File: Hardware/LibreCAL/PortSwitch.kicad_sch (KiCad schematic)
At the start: 20 parts, among them J1 901-10510-2, J2 901-10510-2, J3 901-10510-2, J4 901-10510-2, U1 PE426462, U2 PE426462, U3 PE426462, U4 PE426462

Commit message: Partial routing
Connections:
- net GND: now also U1.20 (NC), U2.20 (NC), U3.20 (NC), U4.20 (NC)
- net at U2.2 (RF2): now also U3.2 (RF2); no longer U4.15 (RF4)
- net at U2.4 (RF3): now also U4.15 (RF4); no longer U3.4 (RF3)
- net at U1.15 (RF4): now also U3.4 (RF3); no longer U3.2 (RF2)
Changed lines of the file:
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@@
   (junction (at 207.01 142.24) (diameter 0) (color 0 0 0 0)
   )
+  (junction (at 72.39 66.04) (diameter 0) (color 0 0 0 0)
+  )
   (junction (at 212.09 142.24) (diameter 0) (color 0 0 0 0)
   )
@@
   (junction (at 100.33 76.2) (diameter 0) (color 0 0 0 0)
   )
+  (junction (at 219.71 66.04) (diameter 0) (color 0 0 0 0)
+  )
   (junction (at 207.01 76.2) (diameter 0) (color 0 0 0 0)
   )
@@
   (junction (at 196.85 76.2) (diameter 0) (color 0 0 0 0)
   )
+  (junction (at 72.39 132.08) (diameter 0) (color 0 0 0 0)
+  )
   (junction (at 92.71 100.33) (diameter 0) (color 0 0 0 0)
   )
@@
   )
   (junction (at 191.77 142.24) (diameter 0) (color 0 0 0 0)
+  )
+  (junction (at 219.71 132.08) (diameter 0) (color 0 0 0 0)
   )
   (junction (at 186.69 142.24) (diameter 0) (color 0 0 0 0)
@@
     (stroke (width 0) (type default) (color 0 0 0 0))
   )
+  (wire (pts (xy 113.03 124.46) (xy 138.43 124.46))
+    (stroke (width 0) (type default) (color 0 0 0 0))
+  )
   (wire (pts (xy 97.79 142.24) (xy 95.25 142.24))
     (stroke (width 0) (type default) (color 0 0 0 0))
@@
     (stroke (width 0) (type default) (color 0 0 0 0))
   )
+  (wire (pts (xy 156.21 58.42) (xy 179.07 58.42))
+    (stroke (width 0) (type default) (color 0 0 0 0))
+  )
   (wire (pts (xy 97.79 140.97) (xy 97.79 142.24))
     (stroke (width 0) (type default) (color 0 0 0 0))
@@
     (stroke (width 0) (type default) (color 0 0 0 0))
   )
-  (wire (pts (xy 156.21 60.96) (xy 156.21 55.88))
-    (stroke (width 0) (type default) (color 0 0 0 0))
-  )
   (wire (pts (xy 179.07 60.96) (xy 161.29 60.96))
     (stroke (width 0) (type default) (color 0 0 0 0))
   )
+  (wire (pts (xy 179.07 55.88) (xy 151.13 55.88))
+    (stroke (width 0) (type default) (color 0 0 0 0))
+  )
+  (wire (pts (xy 72.39 132.08) (xy 74.93 132.08))
+    (stroke (width 0) (type default) (color 0 0 0 0))
+  )
   (wire (pts (xy 102.87 76.2) (xy 100.33 76.2))
     (stroke (width 0) (type default) (color 0 0 0 0))
   )
-  (wire (pts (xy 156.21 55.88) (xy 179.07 55.88))
-    (stroke (width 0) (type default) (color 0 0 0 0))
-  )
   (wire (pts (xy 222.25 63.5) (xy 217.17 63.5))
     (stroke (width 0) (type default) (color 0 0 0 0))
@@
     (stroke (width 0) (type default) (color 0 0 0 0))
   )
+  (wire (pts (xy 72.39 66.04) (xy 74.93 66.04))
+    (stroke (width 0) (type default) (color 0 0 0 0))
+  )
   (wire (pts (xy 199.39 34.29) (xy 199.39 46.99))
     (stroke (width 0) (type default) (color 0 0 0 0))
@@
     (stroke (width 0) (type default) (color 0 0 0 0))
   )
-  (wire (pts (xy 72.39 55.88) (xy 72.39 76.2))
+  (wire (pts (xy 72.39 55.88) (xy 72.39 66.04))
     (stroke (width 0) (type default) (color 0 0 0 0))
   )
@@
     (stroke (width 0) (type default) (color 0 0 0 0))
   )
-  (wire (pts (xy 151.13 58.42) (xy 179.07 58.42))
-    (stroke (width 0) (type default) (color 0 0 0 0))
-  )
-  (wire (pts (xy 219.71 55.88) (xy 219.71 76.2))
+  (wire (pts (xy 113.03 121.92) (xy 138.43 121.92))
+    (stroke (width 0) (type default) (color 0 0 0 0))
+  )
+  (wire (pts (xy 219.71 66.04) (xy 219.71 76.2))
+    (stroke (width 0) (type default) (color 0 0 0 0))
+  )
+  (wire (pts (xy 219.71 55.88) (xy 219.71 66.04))
     (stroke (width 0) (type default) (color 0 0 0 0))
   )
@@
     (stroke (width 0) (type default) (color 0 0 0 0))
   )
+  (wire (pts (xy 72.39 66.04) (xy 72.39 76.2))
+    (stroke (width 0) (type default) (color 0 0 0 0))
+  )
+  (wire (pts (xy 138.43 121.92) (xy 138.43 63.5))
+    (stroke (width 0) (type default) (color 0 0 0 0))
+  )
   (wire (pts (xy 92.71 74.93) (xy 92.71 76.2))
     (stroke (width 0) (type default) (color 0 0 0 0))
@@
     (stroke (width 0) (type default) (color 0 0 0 0))
   )
+  (wire (pts (xy 138.43 124.46) (xy 138.43 127))
+    (stroke (width 0) (type default) (color 0 0 0 0))
+  )
   (wire (pts (xy 90.17 76.2) (xy 87.63 76.2))
     (stroke (width 0) (type default) (color 0 0 0 0))
@@
     (stroke (width 0) (type default) (color 0 0 0 0))
   )
-  (wire (pts (xy 113.03 124.46) (xy 138.43 124.46))
-    (stroke (width 0) (type default) (color 0 0 0 0))
-  )
   (wire (pts (xy 130.81 127) (xy 113.03 127))
     (stroke (width 0) (type default) (color 0 0 0 0))
@@
     (stroke (width 0) (type default) (color 0 0 0 0))
   )
-  (wire (pts (xy 179.07 127) (xy 148.59 127))
+  (wire (pts (xy 138.43 127) (xy 179.07 127))
     (stroke (width 0) (type default) (color 0 0 0 0))
   )
@@
     (stroke (width 0) (type default) (color 0 0 0 0))
   )
+  (wire (pts (xy 217.17 66.04) (xy 219.71 66.04))
+    (stroke (width 0) (type default) (color 0 0 0 0))
+  )
   (wire (pts (xy 199.39 100.33) (xy 199.39 113.03))
     (stroke (width 0) (type default) (color 0 0 0 0))
@@
     (stroke (width 0) (type default) (color 0 0 0 0))
   )
+  (wire (pts (xy 72.39 132.08) (xy 72.39 142.24))
+    (stroke (width 0) (type default) (color 0 0 0 0))
+  )
   (wire (pts (xy 74.93 119.38) (xy 48.26 119.38))
     (stroke (width 0) (type default) (color 0 0 0 0))
@@
     (stroke (width 0) (type default) (color 0 0 0 0))
   )
-  (wire (pts (xy 138.43 124.46) (xy 138.43 63.5))
-    (stroke (width 0) (type default) (color 0 0 0 0))
-  )
   (wire (pts (xy 90.17 140.97) (xy 90.17 142.24))
     (stroke (width 0) (type default) (color 0 0 0 0))
@@
     (stroke (width 0) (type default) (color 0 0 0 0))
   )
-  (wire (pts (xy 151.13 63.5) (xy 151.13 58.42))
+  (wire (pts (xy 151.13 55.88) (xy 151.13 63.5))
     (stroke (width 0) (type default) (color 0 0 0 0))
   )
@@
     (stroke (width 0) (type default) (color 0 0 0 0))
   )
+  (wire (pts (xy 219.71 132.08) (xy 219.71 142.24))
+    (stroke (width 0) (type default) (color 0 0 0 0))
+  )
   (wire (pts (xy 199.39 140.97) (xy 199.39 142.24))
     (stroke (width 0) (type default) (color 0 0 0 0))
@@
     (stroke (width 0) (type default) (color 0 0 0 0))
   )
-  (wire (pts (xy 148.59 127) (xy 148.59 121.92))
+  (wire (pts (xy 217.17 132.08) (xy 219.71 132.08))
     (stroke (width 0) (type default) (color 0 0 0 0))
   )
@@
     (stroke (width 0) (type default) (color 0 0 0 0))
   )
-  (wire (pts (xy 219.71 121.92) (xy 219.71 142.24))
+  (wire (pts (xy 219.71 121.92) (xy 219.71 132.08))
     (stroke (width 0) (type default) (color 0 0 0 0))
   )
@@
     (stroke (width 0) (type default) (color 0 0 0 0))
   )
+  (wire (pts (xy 156.21 58.42) (xy 156.21 60.96))
+    (stroke (width 0) (type default) (color 0 0 0 0))
+  )
   (wire (pts (xy 113.03 53.34) (xy 115.57 53.34))
     (stroke (width 0) (type default) (color 0 0 0 0))
@@
     (stroke (width 0) (type default) (color 0 0 0 0))
   )
-  (wire (pts (xy 148.59 121.92) (xy 113.03 121.92))
-    (stroke (width 0) (type default) (color 0 0 0 0))
-  )
   (wire (pts (xy 102.87 142.24) (xy 100.33 142.24))
     (stroke (width 0) (type default) (color 0 0 0 0))
@@
     (stroke (width 0) (type default) (color 0 0 0 0))
   )
-  (wire (pts (xy 72.39 121.92) (xy 72.39 142.24))
+  (wire (pts (xy 72.39 121.92) (xy 72.39 132.08))
     (stroke (width 0) (type default) (color 0 0 0 0))
   )
@@
     (pin "1")
   )
-  (symbol (lib_id "LibreCAL:PE426462") (at 92.71 124.46 0) (unit 1)
+  (symbol (lib_name "PE426462_2") (lib_id "LibreCAL:PE426462") (at 92.71 124.46 0) (unit 1)
     (in_bom yes) (on_board yes) (fields_autoplaced)
     (property "Reference" "U2" (id 0) (at 94.7294 110.49 0)
@@
     (pin "1")
   )
-  (symbol (lib_id "LibreCAL:PE426462") (at 92.71 58.42 0) (unit 1)
+  (symbol (lib_name "PE426462_1") (lib_id "LibreCAL:PE426462") (at 92.71 58.42 0) (unit 1)
     (in_bom yes) (on_board yes) (fields_autoplaced)
     (property "Reference" "U1" (id 0) (at 94.7294 44.45 0)
@@
     (pin "1")
   )
-  (symbol (lib_id "LibreCAL:PE426462") (at 199.39 58.42 0) (mirror y) (unit 1)
+  (symbol (lib_name "PE426462_3") (lib_id "LibreCAL:PE426462") (at 199.39 58.42 0) (mirror y) (unit 1)
     (in_bom yes) (on_board yes) (fields_autoplaced)
     (property "Reference" "U3" (id 0) (at 197.3706 44.45 0)

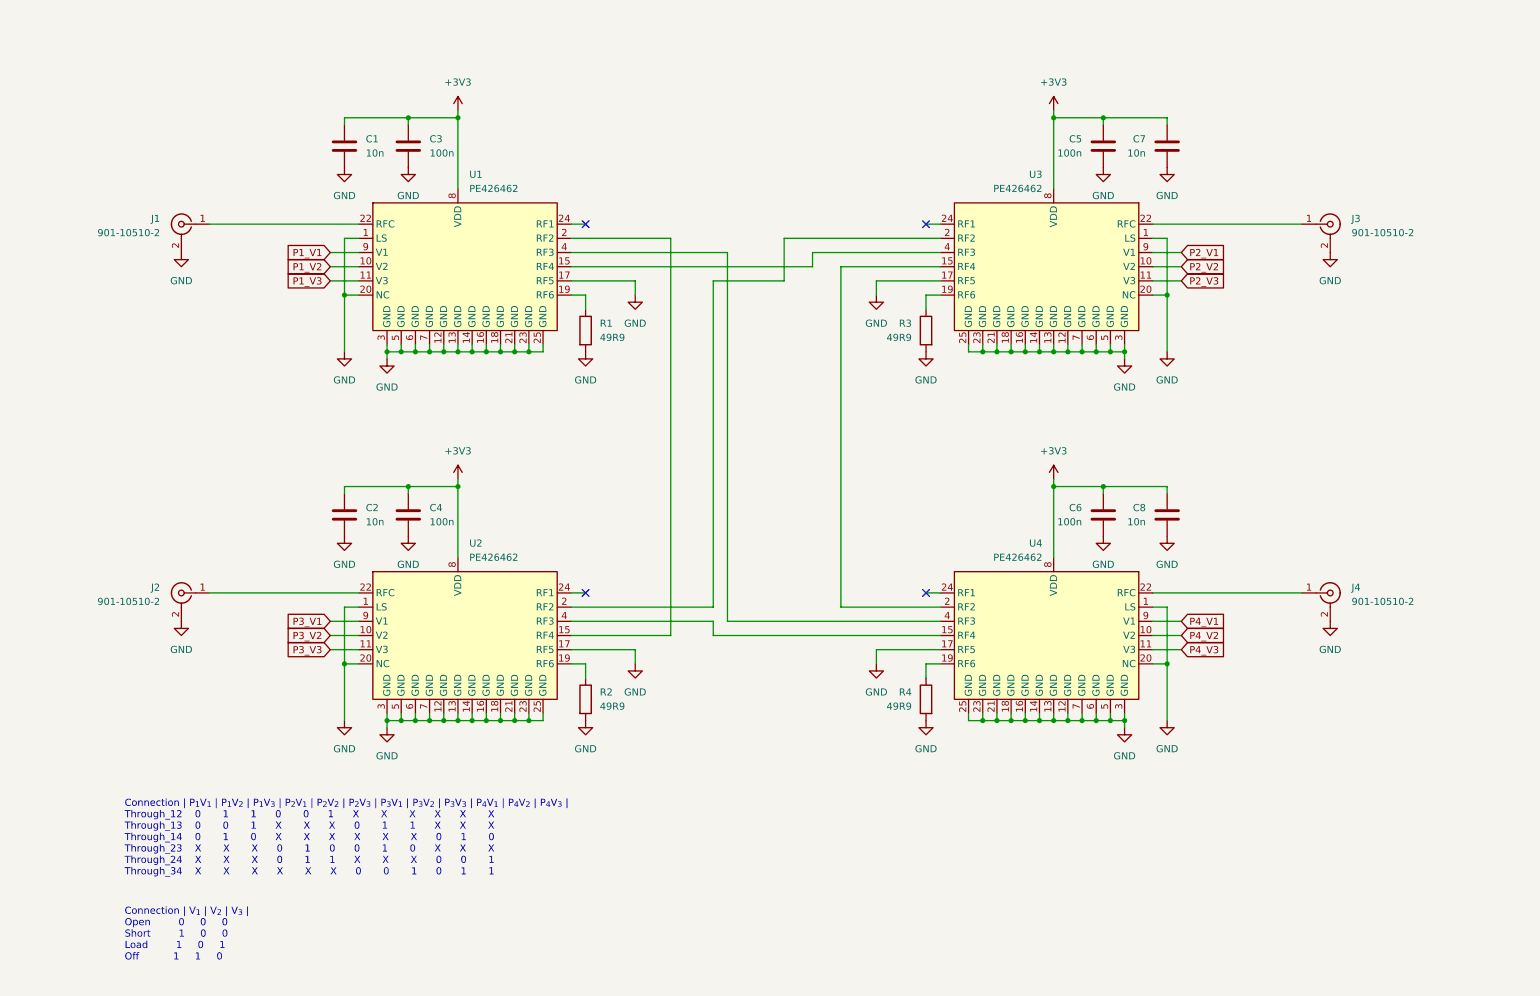
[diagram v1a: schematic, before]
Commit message: Filters added, housing updated
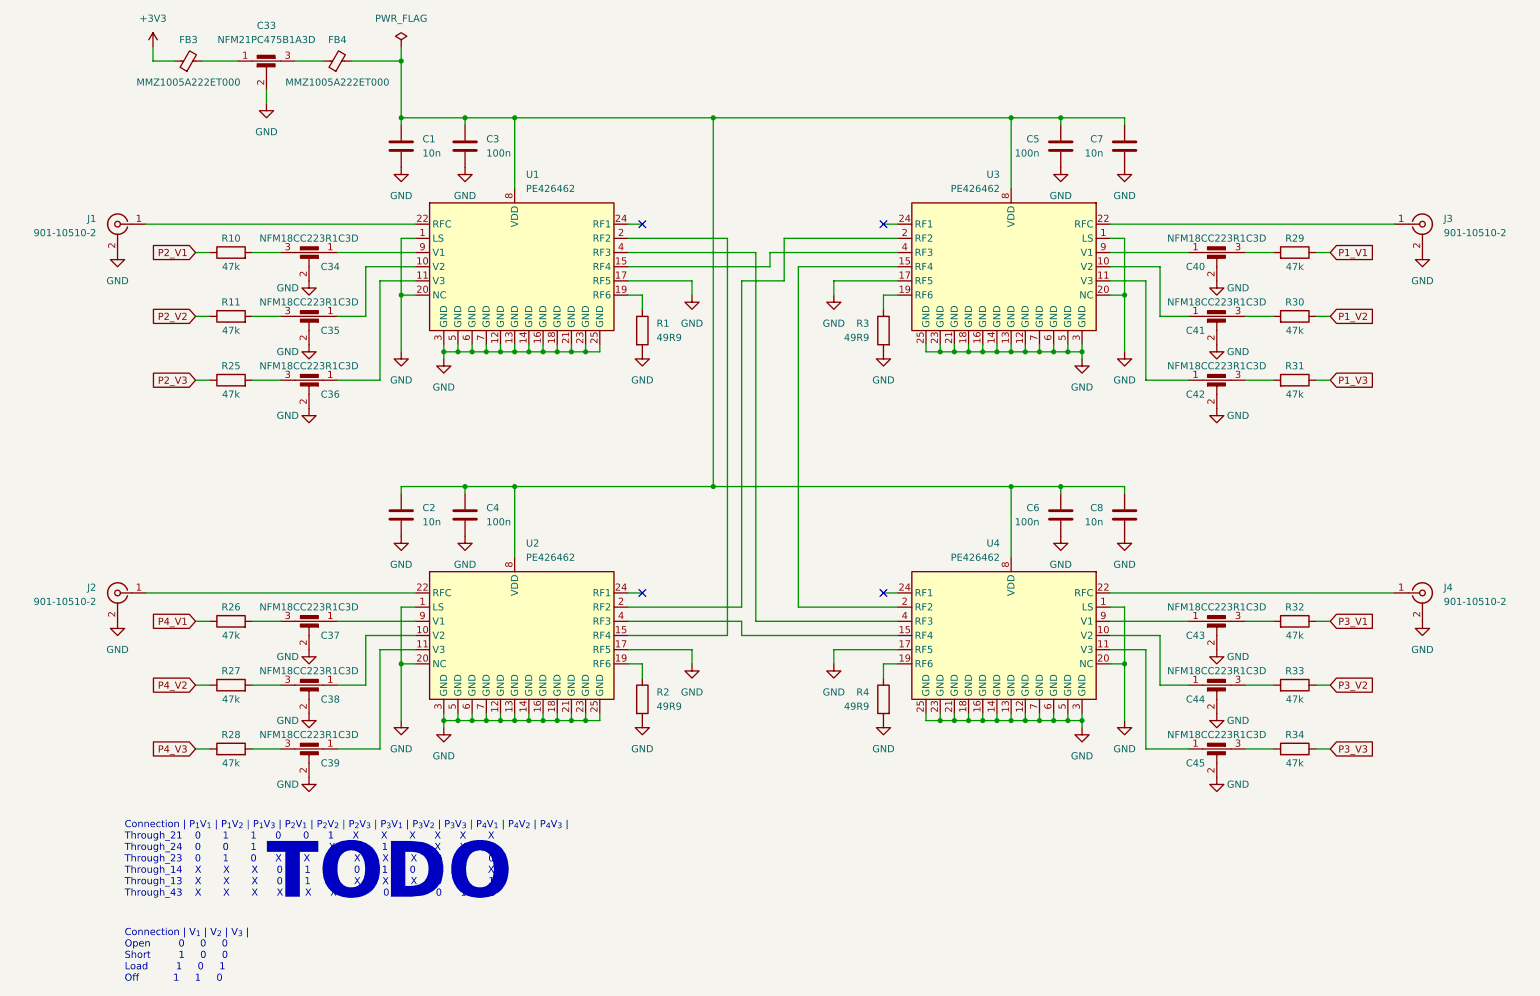
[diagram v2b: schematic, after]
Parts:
- added C33: NFM21PC475B1A3D, LibreCAL:NFM21PC, symbol Device:C_Feedthrough
- added C34, C35, C36, C37, C38, C39, C40, C41, C42, C43, C44, C45: NFM18CC223R1C3D, LibreCAL:NFM18CC, symbol Device:C_Feedthrough
- added FB3, FB4: MMZ1005A222ET000, Inductor_SMD:L_0402_1005Metric, symbol Device:FerriteBead_Small
- added R10, R11, R25, R26, R27, R28, R29, R30, R31, R32, R33, R34: 47k, Resistor_SMD:R_0402_1005Metric, symbol Device:R
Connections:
- net +3V3: now also FB3.1; no longer C1.1, C2.1, C3.1, C4.1, C5.1, C6.1, C7.1, C8.1, U1.8 (VDD), U2.8 (VDD), U3.8 (VDD), U4.8 (VDD)
- net GND: now also C33.2, C34.2, C35.2, C36.2, C37.2, C38.2, C39.2, C40.2, C41.2, C42.2, C43.2, C44.2, C45.2
- net P1_V1: now also R29.1; no longer U1.9 (V1)
- net P1_V2: now also R30.1; no longer U1.10 (V2)
- net P1_V3: now also R31.1; no longer U1.11 (V3)
- net P2_V1: now also R10.1; no longer U3.9 (V1)
- net P2_V2: now also R11.1; no longer U3.10 (V2)
- net P2_V3: now also R25.1; no longer U3.11 (V3)
- net P3_V1: now also R32.1; no longer U2.9 (V1)
- net P3_V2: now also R33.1; no longer U2.10 (V2)
- net P3_V3: now also R34.1; no longer U2.11 (V3)
- net P4_V1: now also R26.1; no longer U4.9 (V1)
- net P4_V2: now also R27.1; no longer U4.10 (V2)
- net P4_V3: now also R28.1; no longer U4.11 (V3)
- new net: C45.3, R34.2
- new net: C1.1, C2.1, C3.1, C4.1, C5.1, C6.1, C7.1, C8.1, FB4.2, U1.8 (VDD), U2.8 (VDD), U3.8 (VDD), U4.8 (VDD)
- new net: C38.1, U2.10 (V2)
- new net: C39.1, U2.11 (V3)
- new net: C37.1, U2.9 (V1)
- new net: C37.3, R26.2
- new net: C43.1, U4.9 (V1)
- new net: C43.3, R32.2
- new net: C40.1, U3.9 (V1)
- new net: C40.3, R29.2
- new net: C45.1, U4.11 (V3)
- new net: C39.3, R28.2
- new net: C33.1, FB3.2
- new net: C33.3, FB4.1
- new net: C35.1, U1.10 (V2)
- new net: C35.3, R11.2
- new net: C42.3, R31.2
- new net: C44.1, U4.10 (V2)
- new net: C34.3, R10.2
- new net: C36.3, R25.2
- new net: C38.3, R27.2
- new net: C36.1, U1.11 (V3)
- new net: C34.1, U1.9 (V1)
- new net: C41.1, U3.10 (V2)
- new net: C42.1, U3.11 (V3)
- new net: C44.3, R33.2
- new net: C41.3, R30.2
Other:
- note added: "Connection | P_{1}V_{1} | P_{1}V_{2} | P_{1}V_{3} | P_{2}V_{1} | P_{2}V_{2} | P_{2}V_{3} | P_{3}V_{1} | P_{3}V_{2} | P_{3}V_{3} | P_{4}V_{1} | P_{4}V_{2} | P_{4}V_{3} | Through_21 0 1 1 0 0 1 X X X X X X Through_24 0 0 1 X X X 0 1 1 X X X Through_23 0 1 0 X X X X X X 0 1 0 Through_14 X X X 0 1 0 0 1 0 X X X Through_13 X X X 0 1 1 X X X 0 0 1 Through_43 X X X X X X 0 0 1 0 1 1"
- note added: "TODO"
- note removed: "Connection | P_{1}V_{1} | P_{1}V_{2} | P_{1}V_{3} | P_{2}V_{1} | P_{2}V_{2} | P_{2}V_{3} | P_{3}V_{1} | P_{3}V_{2} | P_{3}V_{3} | P_{4}V_{1} | P_{4}V_{2} | P_{4}V_{3} | Through_12 0 1 1 0 0 1 X X X X X X Through_13 0 0 1 X X X 0 1 1 X X X Through_14 0 1 0 X X X X X X 0 1 0 Through_23 X X X 0 1 0 0 1 0 X X X Through_24 X X X 0 1 1 X X X 0 0 1 Through_34 X X X X X X 0 0 1 0 1 1"
- moved on the sheet: C1, C2, C3, C4, C5, C6, C7, C8, J1, J2, J3, J4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
